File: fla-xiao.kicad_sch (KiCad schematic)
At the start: 9 parts, among them J1 Conn_PinHeader_1x08_P2.54mm_V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, J2 Conn_PinHeader_1x04_P2.54mm_V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, J3 Conn_PinHeader_2x03_P2.54mm_V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, M1 Module_XIAO-RP2040_SocketSMD, SW1 BUTTON_B3SN

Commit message: Updated board
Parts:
- removed J1: Conn_PinHeader_1x08_P2.54mm_Vertical_THT_D1mm, fab:PinHeader_1x08_P2.54mm_Vertical_THT_D1mm, symbol fab:Conn_PinHeader_1x08_P2.54mm_Vertical_THT_D1mm
- removed J2: Conn_PinHeader_1x04_P2.54mm_Vertical_THT_D1mm, fab:PinHeader_1x04_P2.54mm_Vertical_THT_D1mm, symbol fab:Conn_PinHeader_1x04_P2.54mm_Vertical_THT_D1mm
- added J4: Conn_PinHeader_1x08_P2.54mm_Horizontal_SMD, fab:PinHeader_1x08_P2.54mm_Horizontal_SMD, symbol fab:Conn_PinHeader_1x08_P2.54mm_Horizontal_SMD
- added J5: Conn_PinHeader_1x05_P2.54mm_Horizontal_SMD, fab:PinHeader_1x05_P2.54mm_Horizontal_SMD, symbol fab:Conn_PinHeader_1x05_P2.54mm_Horizontal_SMD
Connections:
- net GND: now also J4.1 (Pin_1), J4.7 (Pin_7), J5.1 (Pin_1)
- net A7: now reaches M1.8 (D7), R2.1, SW1.1
- net A0: now reaches M1.1 (D0)
- net A0: now also J4.5 (Pin_5)
- net A1: now reaches M1.2 (D1)
- net A1: now also J4.4 (Pin_4)
- net A2: now reaches M1.3 (D2)
- net A2: now also J4.3 (Pin_3)
- net A3: now reaches M1.4 (D3)
- net A3: now also J4.2 (Pin_2)
- net A9: now reaches J3.3 (Pin_3), M1.10 (D9)
- net A10: now reaches J3.1 (Pin_1), M1.11 (D10)
- net SDA: now reaches M1.5 (D4)
- net SDA: now also J5.3 (Pin_3)
- net SCL: now reaches M1.6 (D5)
- net SCL: now also J5.4 (Pin_4)
- net A6: now reaches M1.7 (D6), R1.2
- net A8: now reaches J3.5 (Pin_5), M1.9 (D8)
- net +3V3 renamed PWR_3V3
- net PWR_3V3: now also J4.6 (Pin_6), J5.5 (Pin_5)
- net +5V renamed PWR_5V
- net PWR_5V: now also J4.8 (Pin_8), J5.2 (Pin_2)
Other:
- moved on the sheet: D1, J3, R1, R2, R3, SW1

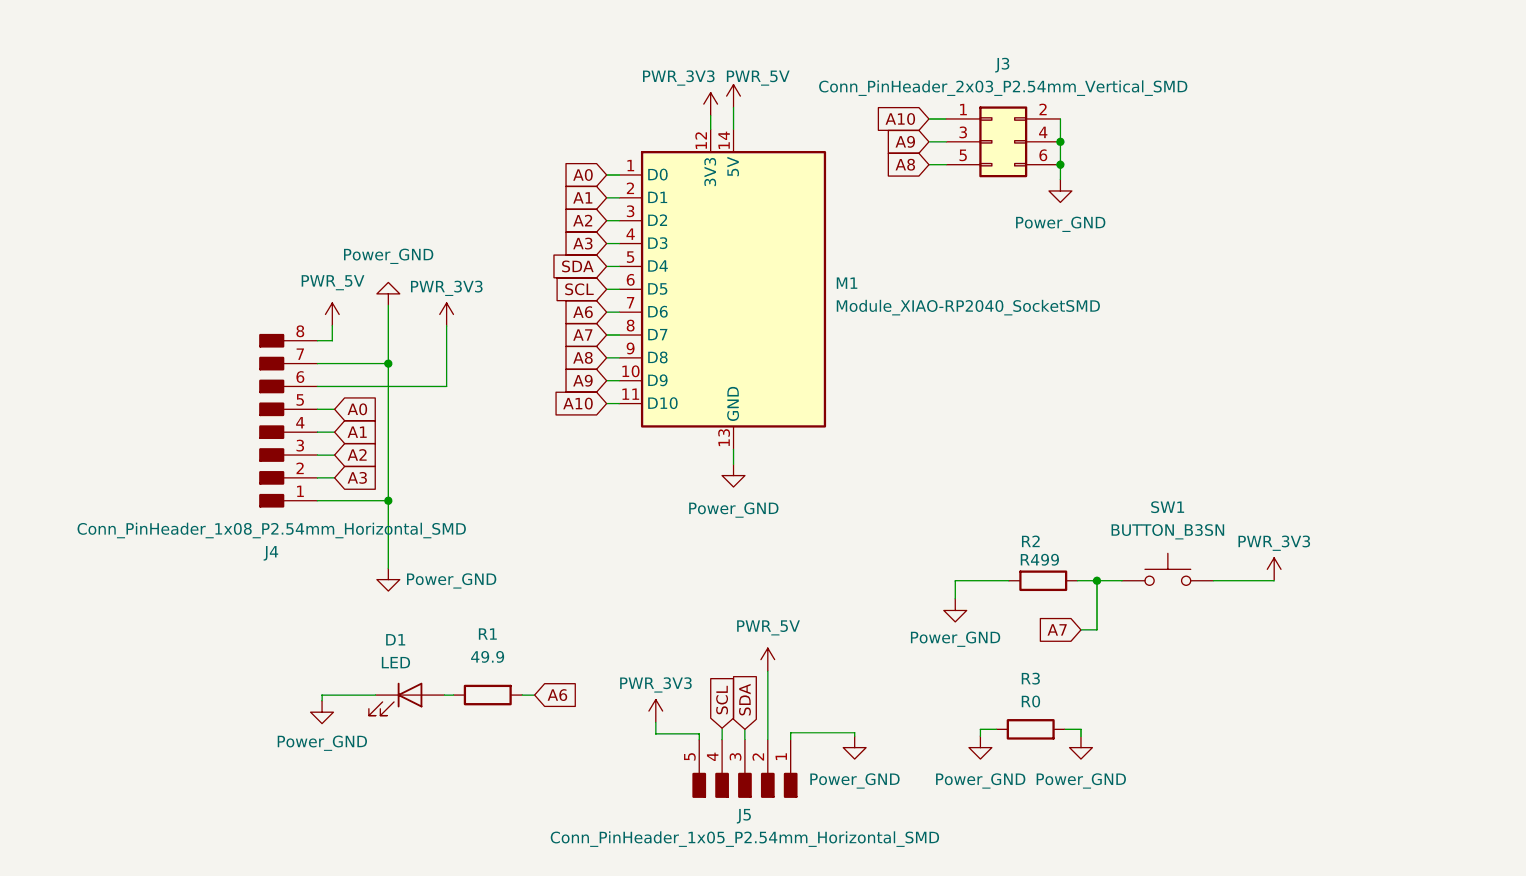
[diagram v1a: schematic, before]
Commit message: Updated images
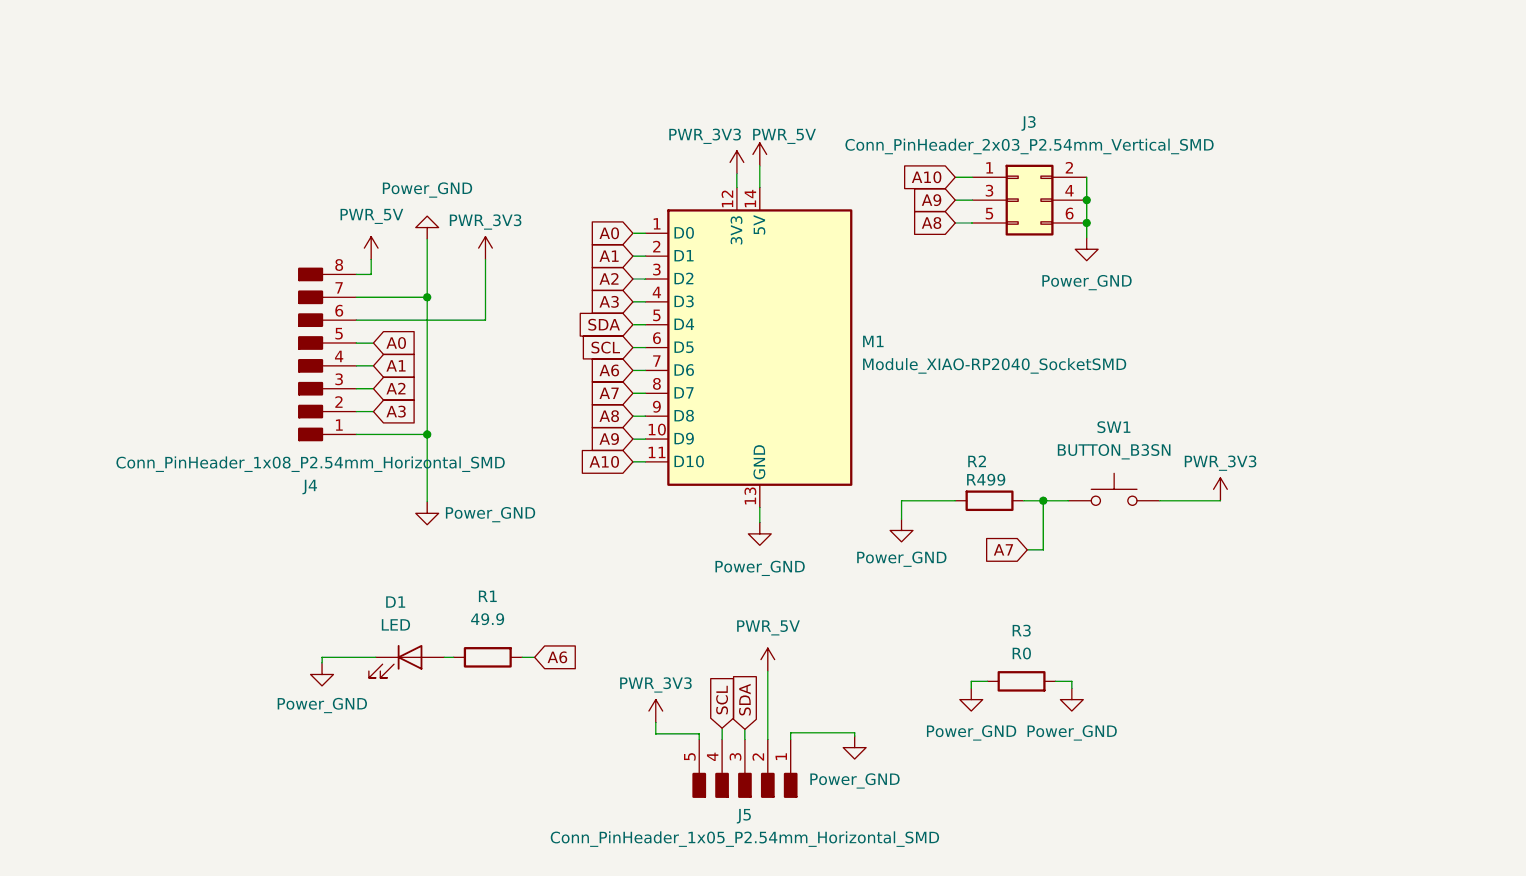
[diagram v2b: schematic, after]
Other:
- moved on the sheet: D1, J3, J4, M1, R1, R2, R3, SW1

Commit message: Updated design, for Xtool Laser
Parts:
- removed R3: R0, fab:R_1206, symbol fab:R
- R1: value 49.9 -> R1K
